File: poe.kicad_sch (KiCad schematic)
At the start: 24 parts, among them Q1 Si4848DY, T1 POE70P-50L, U6 TPS23753

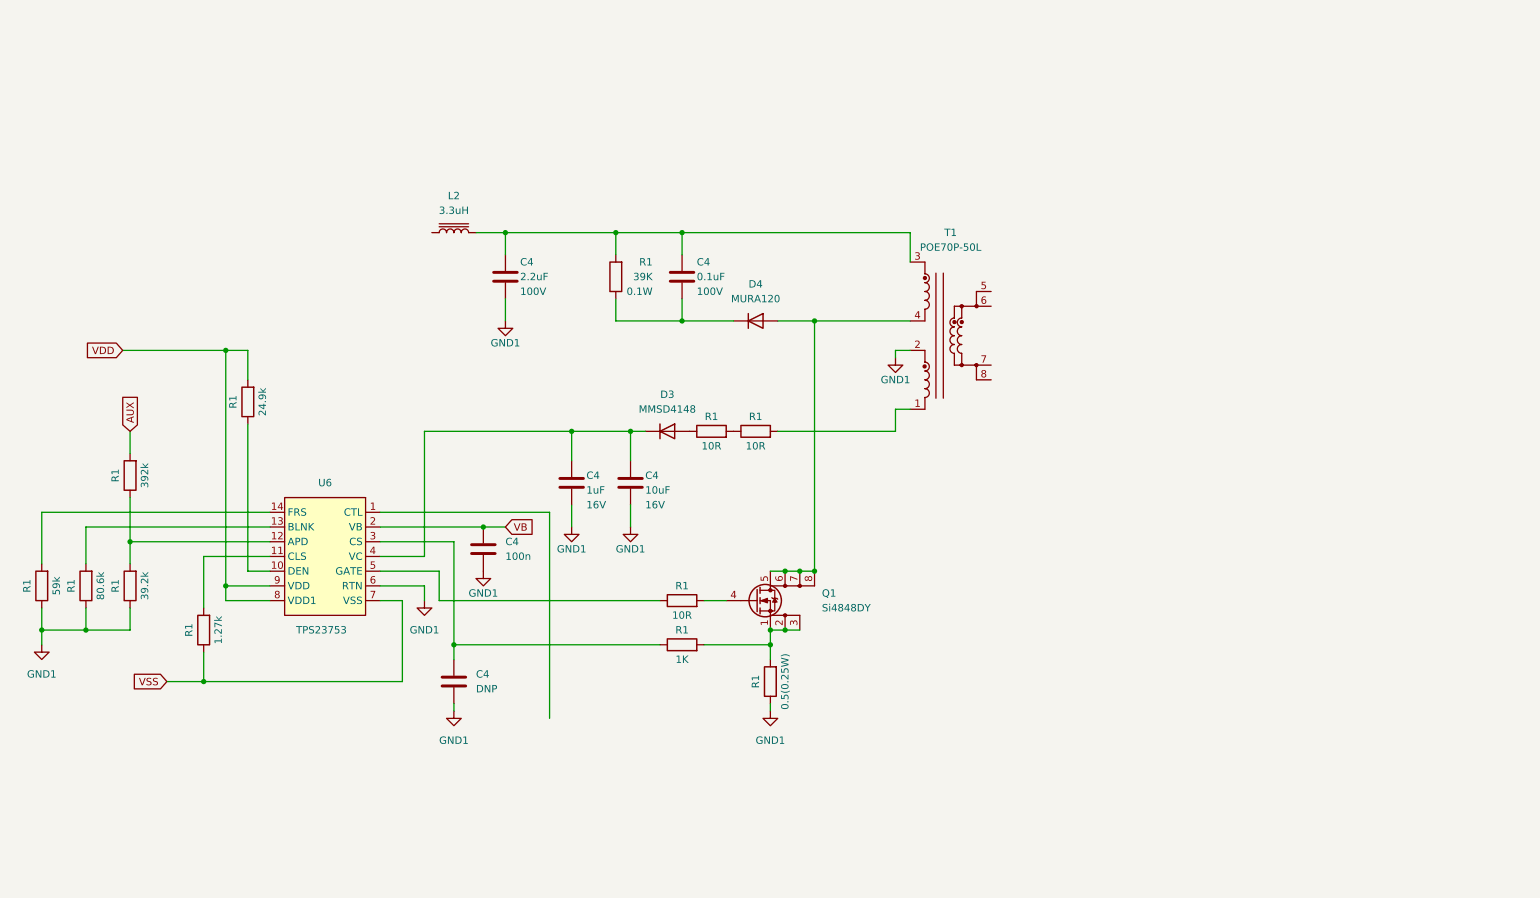
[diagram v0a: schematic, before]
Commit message: add POE schematics, Ethernet phy
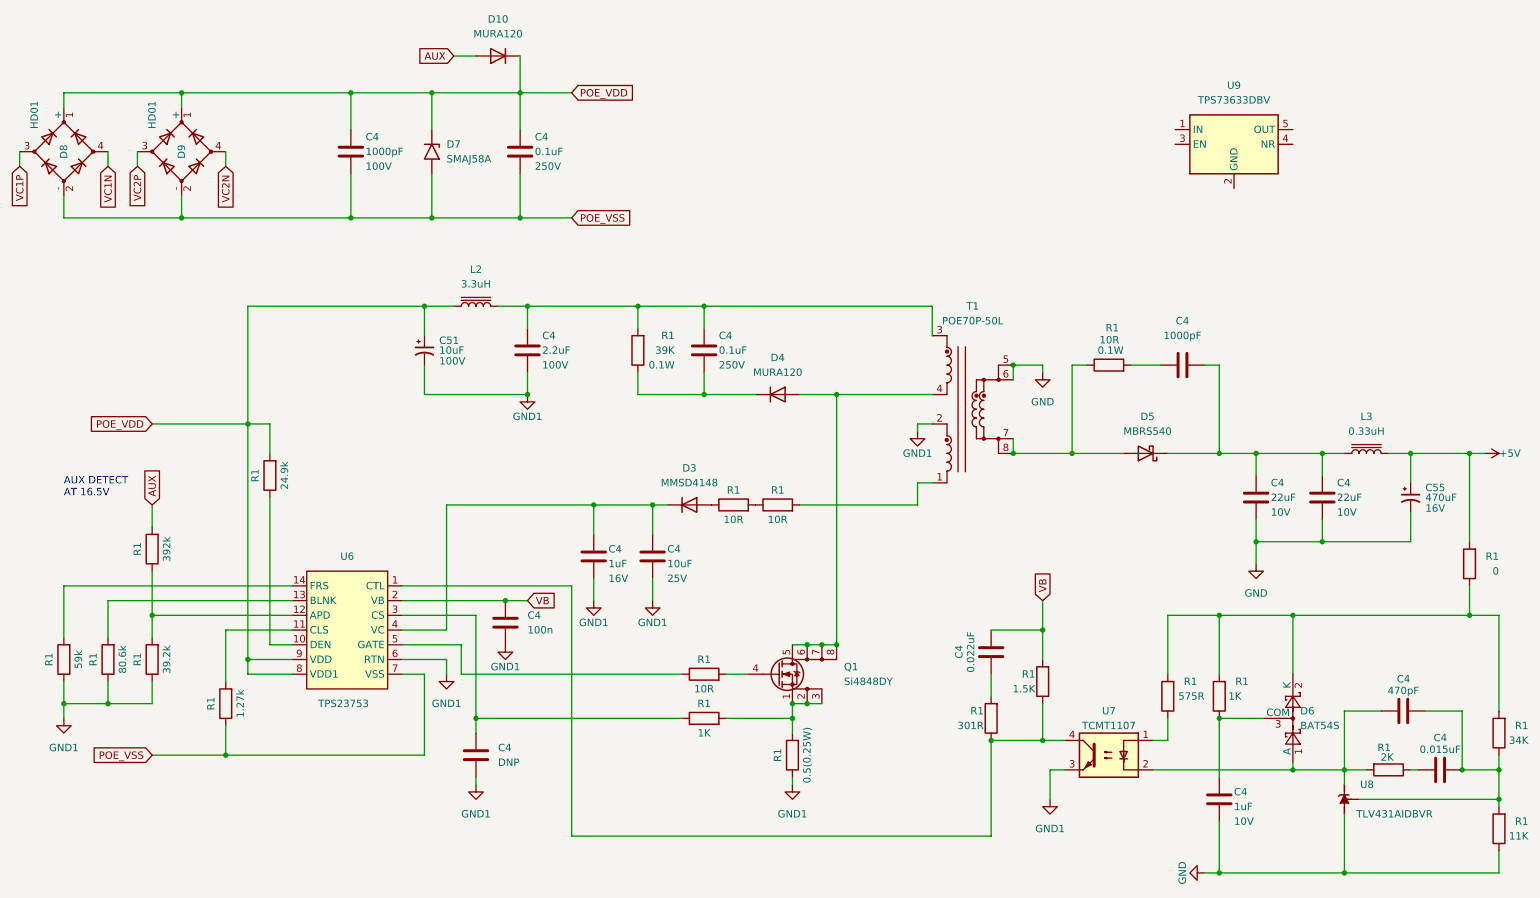
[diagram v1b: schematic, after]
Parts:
- removed C4: 0.1uF, Capacitor_SMD:C_0402_1005Metric, symbol Device:C
- added C4: 0.022uF, Capacitor_SMD:C_0402_1005Metric, symbol Device:C
- added C4: 0.015uF, Capacitor_SMD:C_0603_1608Metric, symbol Device:C
- added C4: 1uF, Capacitor_SMD:C_0402_1005Metric, symbol Device:C
- added C4: 1000pF, Capacitor_SMD:C_0402_1005Metric, symbol Device:C
- added C4 (x2): 0.1uF, Capacitor_SMD:C_0402_1005Metric, symbol Device:C
- added C4 (x2): 22uF, Capacitor_SMD:C_1206_3216Metric, symbol Device:C
- added C4: 1000pF, Capacitor_SMD:C_0805_2012Metric, symbol Device:C
- added C4: 470pF, Capacitor_SMD:C_0603_1608Metric, symbol Device:C
- added C51: 10uF, Capacitor_SMD:C_2220_5650Metric, symbol Device:C_Polarized_Small_US
- added C55: 470uF, Capacitor_SMD:CP_Elec_6.3x7.7, symbol Device:C_Polarized_Small_US
- added D10: MURA120, Diode_SMD:D_SMA, symbol Device:D
- added D5: MBRS540, Diode_SMD:D_SMC, symbol Diode:BAT85
- added D6: BAT54S, Package_TO_SOT_SMD:SOT-23, symbol Diode:BAT54S
- added D7: SMAJ58A, Diode_SMD:D_SMA, symbol Diode:SMAJ58A
- added D8, D9: HD01, Package_TO_SOT_SMD:HD01, symbol Device:D_Bridge_+-AA
- added L3: 0.33uH, Inductor_SMD:L_4.4x4.2_H2, symbol Device:L_Iron
- added R1: 575R, Resistor_SMD:R_0402_1005Metric, symbol Device:R
- added R1: 1K, Resistor_SMD:R_0402_1005Metric, symbol Device:R
- added R1: 1.5K, Resistor_SMD:R_0402_1005Metric, symbol Device:R
- added R1: 34K, Resistor_SMD:R_0402_1005Metric, symbol Device:R
- added R1: 0, Resistor_SMD:R_0402_1005Metric, symbol Device:R
- added R1: 301R, Resistor_SMD:R_0402_1005Metric, symbol Device:R
- added R1: 2K, Resistor_SMD:R_0402_1005Metric, symbol Device:R
- added R1: 10R, Resistor_SMD:R_0402_1005Metric, symbol Device:R
- added R1: 11K, Resistor_SMD:R_0402_1005Metric, symbol Device:R
- added U7: TCMT1107, Package_SO:SOP-4_4.4x2.6mm_P1.27mm, symbol Isolator:TCMT1107
- added U8: TLV431AIDBVR, Package_TO_SOT_SMD:SOT-23-5, symbol Reference_Voltage:TL431DBV
- added U9: TPS73633DBV, Package_TO_SOT_SMD:SOT-23-5, symbol Regulator_Linear:TPS73633DBV
- C4: footprint Capacitor_SMD:C_0402_1005Metric -> Capacitor_SMD:C_0603_1608Metric; Voltage 16V -> 25V
- C4: footprint Capacitor_SMD:C_0402_1005Metric -> Capacitor_SMD:C_0603_1608Metric
- C4: footprint Capacitor_SMD:C_0402_1005Metric -> Capacitor_SMD:C_1206_3216Metric
- L2: footprint Inductor_SMD:L_7.3x7.3_H3.5 -> Inductor_SMD:L_6.6x7.2_H3
- T1: footprint (none) -> Inductor_SMD:POE70P
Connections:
- net VDD is gone; now on net POE_VDD: R1.2, U6.8 (VDD1), U6.9 (VDD)
- net AUX: now also D10.2 (A)
- net GND1: now also C51.2, U7.3
- net VB: now also C4.2, R1.2
- net at C4.1, L2.2, R1.2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: now also C4.1
- net GND: now reaches T1.5
- net GND: now also T1.6, C4.2, C4.2, C4.2, C55.2, R1.1, U8.5 (A)
- net at T1.7: now also T1.8, D5.2 (A), R1.1
- net at U6.1 (CTL): now also R1.1, R1.1, U7.4
- net at D4.1 (K), R1.1: now also C4.2
- net POE_VDD: now reaches L2.1
- net POE_VDD: now also C4.1, C4.1, C51.1, D10.1 (K), D7.1 (A1), D8.1 (+), D9.1 (+)
- net VSS renamed POE_VSS
- net POE_VSS: now also C4.2, C4.2, D7.2 (A2), D8.2 (-), D9.2 (-)
- new net: C4.1, R1.2 (x2)
- new net: C4.1, R1.1
- new net: C4.2, C4.2, R1.1, R1.2, U8.4 (REF)
- new net: R1.1, U7.1
- new net: D6.2 (K), R1.1, R1.2, R1.2, R1.2
- new net: C4.1, D6.3 (COM), R1.1
- new net: C4.1, D6.1 (A), R1.2, U7.2, U8.3 (K)
- new net: C4.1, C4.1, C4.2, D5.1 (K), L3.1
- new net +5V: C55.1, L3.2, R1.2
- new net VC1N: D8.4
- new net VC1P: D8.3
- new net VC2N: D9.4
- new net VC2P: D9.3
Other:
- note added: "AUX DETECT AT 16.5V"
- moved on the sheet: C4, D3, D4, L2, Q1, R1, T1, U6

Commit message: almost final schematics
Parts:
- removed U9: TPS73633DBV, Package_TO_SOT_SMD:SOT-23-5, symbol Regulator_Linear:TPS73633DBV
- added C4 (x3): 1uF, Capacitor_SMD:C_0603_1608Metric, symbol Device:C
- added R1: 100K, Resistor_SMD:R_0603_1608Metric, symbol Device:R
- added R1 (x2): 0, Resistor_SMD:R_0402_1005Metric, symbol Device:R
- added R1: 32K, Resistor_SMD:R_0603_1608Metric, symbol Device:R
- added U14: TLV76733QWDRBxQ1, Package_SON:VSON-8-1EP_3x3mm_P0.65mm_EP1.65x2.4mm, symbol Regulator_Linear:TLV76733QWDRBxQ1
- R1: footprint Resistor_SMD:R_0402_1005Metric -> Resistor_SMD:R_0603_1608Metric
- R1: value 575R -> 575R(500)
- R1: footprint Resistor_SMD:R_0402_1005Metric -> Resistor_SMD:R_0805_2012Metric
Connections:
- net +5V: now also C4.1, R1.2, U14.5 (EN), U14.8 (IN); no longer C55.1, L3.2, R1.2
- net GND: now also C4.2, C4.2, C4.2, R1.1, U14.4 (GND), U14.6 (GND), U14.9 (PAD)
- new net: R1.1, R1.2, U14.3 (SNS)
- new net: C4.1, C4.1, R1.1, R1.2, U14.1 (OUT)
- new net: C55.1, L3.2, R1.1, R1.2
- new net +3.3V: R1.2
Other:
- note added: "R1 + R2 ≤ Vout / (Ifb × Iout) R1 + R2 ≤ 3.3 / (50e-9 * 500) = 132K Ratio R1/R2 (Vfb=0.8) = 3.125;"
